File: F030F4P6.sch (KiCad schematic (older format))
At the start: 11 parts

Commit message: Board update
Added capacitors and extra charge stuff
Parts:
- removed D?: GREEN, symbol Device:LED
- removed D?: RED, symbol Device:LED
- removed R? (x2): 1k5Ω, symbol Device:R
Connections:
- net labels added: Fire_C, Fire_D, Sense_C, Sense_D
- net labels removed: Fet_A, Fet_B
- wire segments 33 -> 27
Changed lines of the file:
@@
 $Descr A4 11693 8268
 encoding utf-8
-Sheet 2 2
+Sheet 2 3
 Title ""
 Date "2021-10-05"
@@
 Wire Notes Line
 	9000 5350 9000 3000
-$Comp
-L Device:R R?
-U 1 1 616146AE
-P 5700 4600
-AR Path="/616146AE" Ref="R?"  Part="1"
-AR Path="/6160DF75/616146AE" Ref="R?"  Part="1"
-F 0 "R?" H 5770 4646 50  0000 L CNN
-F 1 "1k5Ω" H 5770 4555 50  0000 L CNN
-F 2 "" V 5630 4600 50  0001 C CNN
-F 3 "~" H 5700 4600 50  0001 C CNN
-	1    5700 4600
-	1    0    0    -1
-$EndComp
-$Comp
-L power:GND #PWR?
-U 1 1 616146B4
-P 5700 4750
-AR Path="/616146B4" Ref="#PWR?"  Part="1"
-AR Path="/6160DF75/616146B4" Ref="#PWR?"  Part="1"
-F 0 "#PWR?" H 5700 4500 50  0001 C CNN
-F 1 "GND" H 5705 4577 50  0000 C CNN
-F 2 "" H 5700 4750 50  0001 C CNN
-F 3 "" H 5700 4750 50  0001 C CNN
-	1    5700 4750
-	1    0    0    -1
-$EndComp
-$Comp
-L Device:LED D?
-U 1 1 616146BA
-P 5700 4200
-AR Path="/616146BA" Ref="D?"  Part="1"
-AR Path="/6160DF75/616146BA" Ref="D?"  Part="1"
-F 0 "D?" V 5739 4082 50  0000 R CNN
-F 1 "GREEN" V 5648 4082 50  0000 R CNN
-F 2 "" H 5700 4200 50  0001 C CNN
-F 3 "~" H 5700 4200 50  0001 C CNN
-	1    5700 4200
-	0    -1   -1   0
-$EndComp
-$Comp
-L Device:LED D?
-U 1 1 616146C0
-P 5350 4200
-AR Path="/616146C0" Ref="D?"  Part="1"
-AR Path="/6160DF75/616146C0" Ref="D?"  Part="1"
-F 0 "D?" V 5389 4082 50  0000 R CNN
-F 1 "RED" V 5298 4082 50  0000 R CNN
-F 2 "" H 5350 4200 50  0001 C CNN
-F 3 "~" H 5350 4200 50  0001 C CNN
-	1    5350 4200
-	0    -1   -1   0
-$EndComp
-$Comp
-L Device:R R?
-U 1 1 616146C6
-P 5350 4600
-AR Path="/616146C6" Ref="R?"  Part="1"
-AR Path="/6160DF75/616146C6" Ref="R?"  Part="1"
-F 0 "R?" H 5420 4646 50  0000 L CNN
-F 1 "1k5Ω" H 5420 4555 50  0000 L CNN
-F 2 "" V 5280 4600 50  0001 C CNN
-F 3 "~" H 5350 4600 50  0001 C CNN
-	1    5350 4600
-	1    0    0    -1
-$EndComp
-$Comp
-L power:GND #PWR?
-U 1 1 616146CC
-P 5350 4750
-AR Path="/616146CC" Ref="#PWR?"  Part="1"
-AR Path="/6160DF75/616146CC" Ref="#PWR?"  Part="1"
-F 0 "#PWR?" H 5350 4500 50  0001 C CNN
-F 1 "GND" H 5355 4577 50  0000 C CNN
-F 2 "" H 5350 4750 50  0001 C CNN
-F 3 "" H 5350 4750 50  0001 C CNN
-	1    5350 4750
-	1    0    0    -1
-$EndComp
-Wire Wire Line
-	5350 4450 5350 4350
-Wire Wire Line
-	5700 4450 5700 4350
-Wire Wire Line
-	5350 4050 5350 3800
-Wire Wire Line
-	5350 3800 6350 3800
-Wire Wire Line
-	6350 3900 5700 3900
-Wire Wire Line
-	5700 3900 5700 4050
 Wire Notes Line
 	5200 3000 5200 5350
@@
 Wire Notes Line
 	5200 3000 9000 3000
-Text HLabel 6350 4000 0    50   Input ~ 0
+Text HLabel 6350 3800 0    50   Input ~ 0
 Sense_A
 Text HLabel 7350 4100 2    50   Input ~ 0
@@
 Text HLabel 6350 4700 0    50   Input ~ 0
 NRST
-Text HLabel 6350 4100 0    50   Input ~ 0
+Text HLabel 6350 3900 0    50   Input ~ 0
 Sense_B
 Text HLabel 6350 4200 0    50   Input ~ 0
-Fet_A
+Fire_A
 Text HLabel 6350 4300 0    50   Input ~ 0
-Fet_B
-Text HLabel 6350 4400 0    50   Input ~ 0
-Fire_A
-Text HLabel 6350 4500 0    50   Input ~ 0
 Fire_B
 Text HLabel 7350 4000 2    50   Input ~ 0
 Buzzer_Excitation
+Text HLabel 6350 4000 0    50   Input ~ 0
+Sense_C
+Text HLabel 6350 4100 0    50   Input ~ 0
+Sense_D
+Text HLabel 6350 4400 0    50   Input ~ 0
+Fire_C
+Text HLabel 6350 4500 0    50   Input ~ 0
+Fire_D
 $EndSCHEMATC

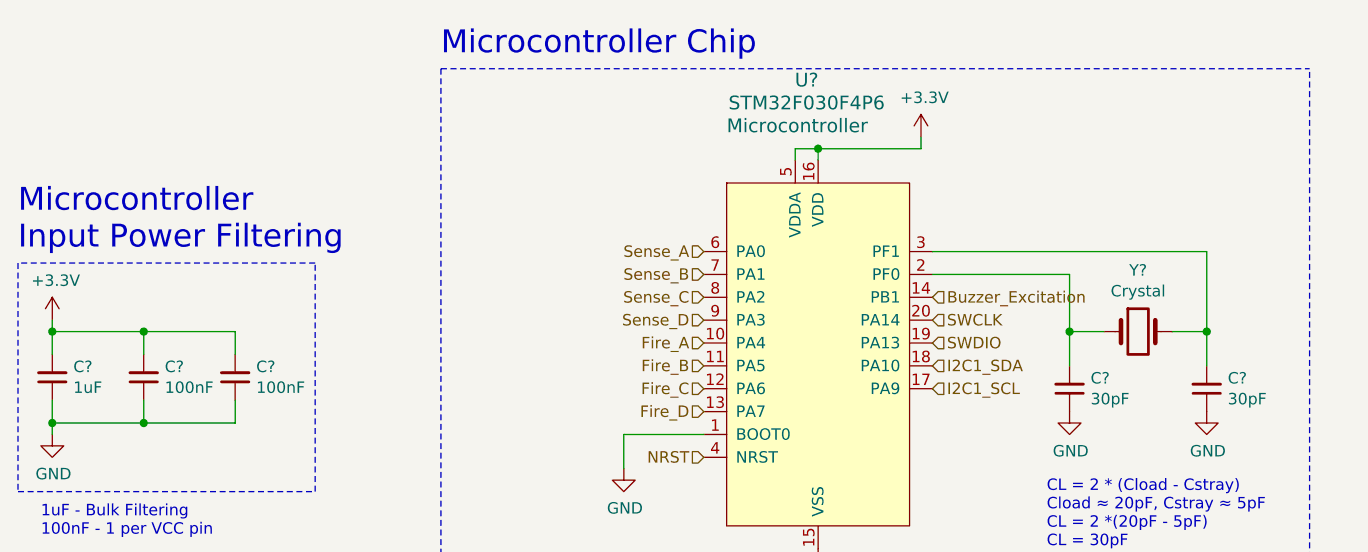
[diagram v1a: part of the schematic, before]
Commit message: Edit to bus
Bus changed as well as some other things to almost finish it up
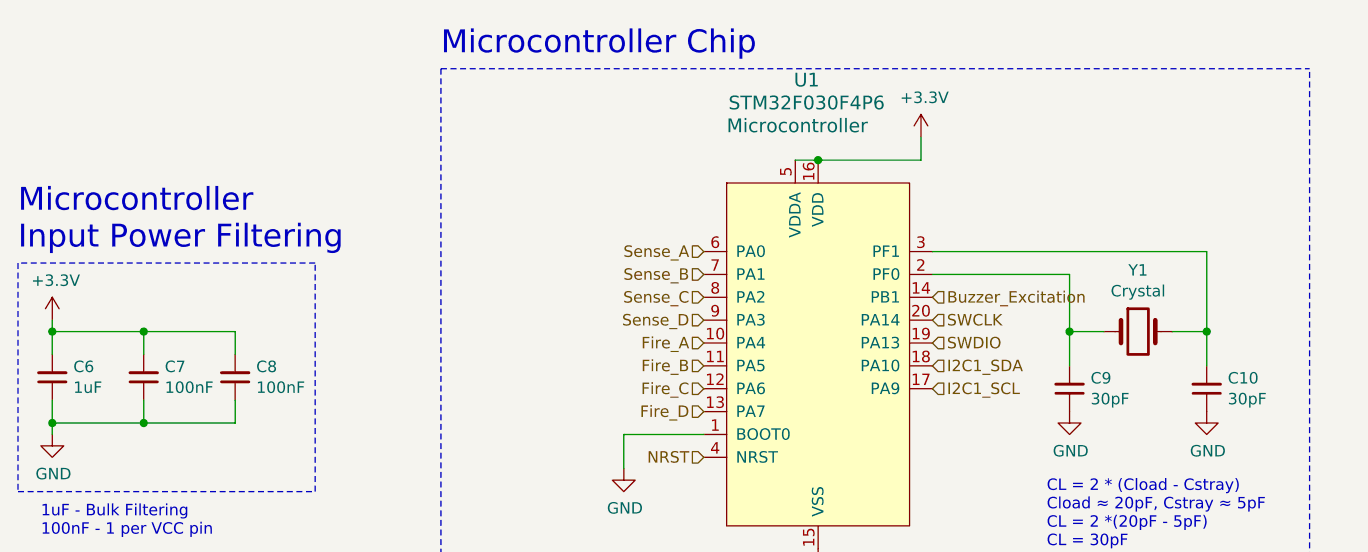
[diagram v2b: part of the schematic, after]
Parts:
- gave numbers to parts that had none: 7
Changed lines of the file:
@@
 $Descr A4 11693 8268
 encoding utf-8
-Sheet 2 3
+Sheet 3 4
 Title ""
 Date "2021-10-05"
@@
 $EndDescr
 $Comp
-L dk_Embedded-Microcontrollers:STM32F030F4P6 U?
-U 1 1 61614629
-P 6750 3900
-AR Path="/61614629" Ref="U?"  Part="1"
-AR Path="/6160DF75/61614629" Ref="U?"  Part="1"
-F 0 "U?" H 6800 4750 60  0000 C CNN
-F 1 "STM32F030F4P6" H 6800 4650 60  0000 C CNN
-F 2 "digikey-footprints:TSSOP-20_W4.4mm" H 6950 4100 60  0001 L CNN
-F 3 "http://www.st.com/content/ccc/resource/technical/document/datasheet/a4/5d/0b/0e/87/c4/4d/71/DM00088500.pdf/files/DM00088500.pdf/jcr:content/translations/en.DM00088500.pdf" H 6950 4200 60  0001 L CNN
-F 4 "497-14044-5-ND" H 6950 4300 60  0001 L CNN "Digi-Key_PN"
-F 5 "STM32F030F4P6" H 6950 4400 60  0001 L CNN "MPN"
-F 6 "Integrated Circuits (ICs)" H 6950 4500 60  0001 L CNN "Category"
-F 7 "Embedded - Microcontrollers" H 6950 4600 60  0001 L CNN "Family"
-F 8 "http://www.st.com/content/ccc/resource/technical/document/datasheet/a4/5d/0b/0e/87/c4/4d/71/DM00088500.pdf/files/DM00088500.pdf/jcr:content/translations/en.DM00088500.pdf" H 6950 4700 60  0001 L CNN "DK_Datasheet_Link"
-F 9 "/product-detail/en/stmicroelectronics/STM32F030F4P6/497-14044-5-ND/4357517" H 6950 4800 60  0001 L CNN "DK_Detail_Page"
-F 10 "Microcontroller" H 6450 4550 60  0000 L CNN "Description"
-F 11 "STMicroelectronics" H 6950 5000 60  0001 L CNN "Manufacturer"
-F 12 "Active" H 6950 5100 60  0001 L CNN "Status"
-	1    6750 3900
-	1    0    0    -1
-$EndComp
-$Comp
 L power:GND #PWR?
 U 1 1 6161462F
 P 6850 5100
 AR Path="/6161462F" Ref="#PWR?"  Part="1"
-AR Path="/6160DF75/6161462F" Ref="#PWR?"  Part="1"
-F 0 "#PWR?" H 6850 4850 50  0001 C CNN
+AR Path="/6160DF75/6161462F" Ref="#PWR0128"  Part="1"
+F 0 "#PWR0128" H 6850 4850 50  0001 C CNN
 F 1 "GND" H 6855 4927 50  0000 C CNN
 F 2 "" H 6850 5100 50  0001 C CNN
@@
 	1    0    0    -1
 $EndComp
-Wire Wire Line
-	7300 3300 7300 3350
-Wire Wire Line
-	7300 3350 6850 3350
-Wire Wire Line
-	6750 3350 6750 3400
-Wire Wire Line
-	6850 3400 6850 3350
-Connection ~ 6850 3350
-Wire Wire Line
-	6850 3350 6750 3350
 $Comp
 L power:+3.3V #PWR?
@@
 P 7300 3300
 AR Path="/6161463B" Ref="#PWR?"  Part="1"
-AR Path="/6160DF75/6161463B" Ref="#PWR?"  Part="1"
-F 0 "#PWR?" H 7300 3150 50  0001 C CNN
+AR Path="/6160DF75/6161463B" Ref="#PWR0129"  Part="1"
+F 0 "#PWR0129" H 7300 3150 50  0001 C CNN
 F 1 "+3.3V" H 7315 3473 50  0000 C CNN
 F 2 "" H 7300 3300 50  0001 C CNN
@@
 P 8250 4150
 AR Path="/61614642" Ref="Y?"  Part="1"
-AR Path="/6160DF75/61614642" Ref="Y?"  Part="1"
-F 0 "Y?" H 8250 4418 50  0000 C CNN
+AR Path="/6160DF75/61614642" Ref="Y1"  Part="1"
+F 0 "Y1" H 8250 4418 50  0000 C CNN
 F 1 "Crystal" H 8250 4327 50  0000 C CNN
 F 2 "" H 8250 4150 50  0001 C CNN
@@
 P 8550 4400
 AR Path="/61614648" Ref="C?"  Part="1"
-AR Path="/6160DF75/61614648" Ref="C?"  Part="1"
-F 0 "C?" H 8458 4354 50  0000 R CNN
+AR Path="/6160DF75/61614648" Ref="C10"  Part="1"
+F 0 "C10" H 8458 4354 50  0000 R CNN
 F 1 "30pF" H 8458 4445 50  0000 R CNN
 F 2 "" H 8550 4400 50  0001 C CNN
@@
 P 7950 4400
 AR Path="/6161464E" Ref="C?"  Part="1"
-AR Path="/6160DF75/6161464E" Ref="C?"  Part="1"
-F 0 "C?" H 7858 4354 50  0000 R CNN
+AR Path="/6160DF75/6161464E" Ref="C9"  Part="1"
+F 0 "C9" H 7858 4354 50  0000 R CNN
 F 1 "30pF" H 7858 4445 50  0000 R CNN
 F 2 "" H 7950 4400 50  0001 C CNN
@@
 P 7950 4500
 AR Path="/61614655" Ref="#PWR?"  Part="1"
-AR Path="/6160DF75/61614655" Ref="#PWR?"  Part="1"
-F 0 "#PWR?" H 7950 4250 50  0001 C CNN
+AR Path="/6160DF75/61614655" Ref="#PWR0130"  Part="1"
+F 0 "#PWR0130" H 7950 4250 50  0001 C CNN
 F 1 "GND" H 7955 4327 50  0000 C CNN
 F 2 "" H 7950 4500 50  0001 C CNN
@@
 P 8550 4500
 AR Path="/6161465B" Ref="#PWR?"  Part="1"
-AR Path="/6160DF75/6161465B" Ref="#PWR?"  Part="1"
-F 0 "#PWR?" H 8550 4250 50  0001 C CNN
+AR Path="/6160DF75/6161465B" Ref="#PWR0131"  Part="1"
+F 0 "#PWR0131" H 8550 4250 50  0001 C CNN
 F 1 "GND" H 8555 4327 50  0000 C CNN
 F 2 "" H 8550 4500 50  0001 C CNN
@@
 P 6000 4750
 AR Path="/61614661" Ref="#PWR?"  Part="1"
-AR Path="/6160DF75/61614661" Ref="#PWR?"  Part="1"
-F 0 "#PWR?" H 6000 4500 50  0001 C CNN
+AR Path="/6160DF75/61614661" Ref="#PWR0132"  Part="1"
+F 0 "#PWR0132" H 6000 4500 50  0001 C CNN
 F 1 "GND" H 6005 4577 50  0000 C CNN
 F 2 "" H 6000 4750 50  0001 C CNN
@@
 P 3500 4350
 AR Path="/61614678" Ref="C?"  Part="1"
-AR Path="/6160DF75/61614678" Ref="C?"  Part="1"
-F 0 "C?" H 3408 4304 50  0000 R CNN
+AR Path="/6160DF75/61614678" Ref="C6"  Part="1"
+F 0 "C6" H 3408 4304 50  0000 R CNN
 F 1 "1uF" H 3408 4395 50  0000 R CNN
 F 2 "" H 3500 4350 50  0001 C CNN
@@
 P 3900 4350
 AR Path="/6161467E" Ref="C?"  Part="1"
-AR Path="/6160DF75/6161467E" Ref="C?"  Part="1"
-F 0 "C?" H 3808 4304 50  0000 R CNN
+AR Path="/6160DF75/6161467E" Ref="C7"  Part="1"
+F 0 "C7" H 3808 4304 50  0000 R CNN
 F 1 "100nF" H 3808 4395 50  0000 R CNN
 F 2 "" H 3900 4350 50  0001 C CNN
@@
 P 4300 4350
 AR Path="/61614684" Ref="C?"  Part="1"
-AR Path="/6160DF75/61614684" Ref="C?"  Part="1"
-F 0 "C?" H 4208 4304 50  0000 R CNN
+AR Path="/6160DF75/61614684" Ref="C8"  Part="1"
+F 0 "C8" H 4208 4304 50  0000 R CNN
 F 1 "100nF" H 4208 4395 50  0000 R CNN
 F 2 "" H 4300 4350 50  0001 C CNN
@@
 P 3500 4600
 AR Path="/6161468A" Ref="#PWR?"  Part="1"
-AR Path="/6160DF75/6161468A" Ref="#PWR?"  Part="1"
-F 0 "#PWR?" H 3500 4350 50  0001 C CNN
+AR Path="/6160DF75/6161468A" Ref="#PWR0133"  Part="1"
+F 0 "#PWR0133" H 3500 4350 50  0001 C CNN
 F 1 "GND" H 3505 4427 50  0000 C CNN
 F 2 "" H 3500 4600 50  0001 C CNN
@@
 P 3500 4100
 AR Path="/61614698" Ref="#PWR?"  Part="1"
-AR Path="/6160DF75/61614698" Ref="#PWR?"  Part="1"
-F 0 "#PWR?" H 3500 3950 50  0001 C CNN
+AR Path="/6160DF75/61614698" Ref="#PWR0134"  Part="1"
+F 0 "#PWR0134" H 3500 3950 50  0001 C CNN
 F 1 "+3.3V" H 3515 4273 50  0000 C CNN
 F 2 "" H 3500 4100 50  0001 C CNN
@@
 Text HLabel 7350 4200 2    50   Input ~ 0
 SWDIO
-Text HLabel 7350 4300 2    50   Input ~ 0
-I2C1_SDA
 Text HLabel 7350 4400 2    50   Input ~ 0
 I2C1_SCL
@@
 Text HLabel 6350 4500 0    50   Input ~ 0
 Fire_D
+$Comp
+L dk_Embedded-Microcontrollers:STM32F030F4P6 U?
+U 1 1 61614629
+P 6750 3900
+AR Path="/61614629" Ref="U?"  Part="1"
+AR Path="/6160DF75/61614629" Ref="U1"  Part="1"
+F 0 "U1" H 6800 4750 60  0000 C CNN
+F 1 "STM32F030F4P6" H 6800 4650 60  0000 C CNN
+F 2 "digikey-footprints:TSSOP-20_W4.4mm" H 6950 4100 60  0001 L CNN
+F 3 "http://www.st.com/content/ccc/resource/technical/document/datasheet/a4/5d/0b/0e/87/c4/4d/71/DM00088500.pdf/files/DM00088500.pdf/jcr:content/translations/en.DM00088500.pdf" H 6950 4200 60  0001 L CNN
+F 4 "497-14044-5-ND" H 6950 4300 60  0001 L CNN "Digi-Key_PN"
+F 5 "STM32F030F4P6" H 6950 4400 60  0001 L CNN "MPN"
+F 6 "Integrated Circuits (ICs)" H 6950 4500 60  0001 L CNN "Category"
+F 7 "Embedded - Microcontrollers" H 6950 4600 60  0001 L CNN "Family"
+F 8 "http://www.st.com/content/ccc/resource/technical/document/datasheet/a4/5d/0b/0e/87/c4/4d/71/DM00088500.pdf/files/DM00088500.pdf/jcr:content/translations/en.DM00088500.pdf" H 6950 4700 60  0001 L CNN "DK_Datasheet_Link"
+F 9 "/product-detail/en/stmicroelectronics/STM32F030F4P6/497-14044-5-ND/4357517" H 6950 4800 60  0001 L CNN "DK_Detail_Page"
+F 10 "Microcontroller" H 6450 4550 60  0000 L CNN "Description"
+F 11 "STMicroelectronics" H 6950 5000 60  0001 L CNN "Manufacturer"
+F 12 "Active" H 6950 5100 60  0001 L CNN "Status"
+	1    6750 3900
+	1    0    0    -1
+$EndComp
+Wire Wire Line
+	6750 3400 6850 3400
+Text HLabel 7350 4300 2    50   Input ~ 0
+I2C1_SDA
+Wire Wire Line
+	6850 3400 7300 3400
+Wire Wire Line
+	7300 3300 7300 3400
+Connection ~ 6850 3400
 $EndSCHEMATC
